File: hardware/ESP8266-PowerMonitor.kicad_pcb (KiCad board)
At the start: 2 copper layers, 31 x 47 mm, 8 parts, among them P1 CONN_01X15, P2 CONN_01X15, P3 CONN_01X02, P4 CONN_01X03, P5 CONN_01X03, P6 CONN_01X03

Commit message: Production prints.
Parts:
- removed the P1 at (143.0, 67.0)
- removed the P2 at (170.0, 67.0)
- removed the P3 at (163.5, 87.5)
- removed the P4 at (150.2, 97.5)
- removed the P5 at (162.5, 97.5)
- removed the P6 at (153.8, 92.8)
- removed the R1 at (153.0, 81.8)
- removed the R2 at (156.2, 81.8)
- added P1: CONN_LEFT, Socket_Strips:Socket_Strip_Straight_1x15, F.Cu at (142.8, 116.8)
- added P1: CONN_LEFT, Socket_Strips:Socket_Strip_Straight_1x15, F.Cu at (177.0, 116.8)
- added P1: CONN_LEFT, Socket_Strips:Socket_Strip_Straight_1x15, F.Cu at (177.2, 68.5)
- added P1: CONN_LEFT, Socket_Strips:Socket_Strip_Straight_1x15, F.Cu at (143.0, 68.5)
- added P2: CONN_RIGHT, Socket_Strips:Socket_Strip_Straight_1x15, F.Cu at (169.5, 116.8)
- added P2: CONN_RIGHT, Socket_Strips:Socket_Strip_Straight_1x15, F.Cu at (203.8, 116.8)
- added P2: CONN_RIGHT, Socket_Strips:Socket_Strip_Straight_1x15, F.Cu at (204.0, 68.5)
- added P2: CONN_RIGHT, Socket_Strips:Socket_Strip_Straight_1x15, F.Cu at (169.8, 68.5)
- added P3: CONN_METER, Pin_Headers:Pin_Header_Straight_1x02, F.Cu at (164.8, 134.8)
- added P3: CONN_METER, Pin_Headers:Pin_Header_Straight_1x02, F.Cu at (199.0, 134.8)
- added P3: CONN_METER, Pin_Headers:Pin_Header_Straight_1x02, F.Cu at (199.2, 86.5)
- added P3: CONN_METER, Pin_Headers:Pin_Header_Straight_1x02, F.Cu at (165.0, 86.5)
- added P4: CONN_PIR, Pin_Headers:Pin_Header_Straight_1x03, F.Cu at (148.5, 121.8)
- added P4: CONN_PIR, Pin_Headers:Pin_Header_Straight_1x03, F.Cu at (182.8, 121.8)
- added P4: CONN_PIR, Pin_Headers:Pin_Header_Straight_1x03, F.Cu at (183.0, 73.5)
- added P4: CONN_PIR, Pin_Headers:Pin_Header_Straight_1x03, F.Cu at (148.8, 73.5)
- added P5: CONN_POWER, Pin_Headers:Pin_Header_Straight_1x03, F.Cu at (148.8, 147.2)
- added P5: CONN_POWER, Pin_Headers:Pin_Header_Straight_1x03, F.Cu at (183.0, 147.2)
- added P5: CONN_POWER, Pin_Headers:Pin_Header_Straight_1x03, F.Cu at (183.2, 99.0)
- added P5: CONN_POWER, Pin_Headers:Pin_Header_Straight_1x03, F.Cu at (149.0, 99.0)
- added P6: CONN_1WIRE, Pin_Headers:Pin_Header_Straight_1x03, F.Cu at (164.8, 143.2)
- added P6: CONN_1WIRE, Pin_Headers:Pin_Header_Straight_1x03, F.Cu at (199.0, 143.2)
- added P6: CONN_1WIRE, Pin_Headers:Pin_Header_Straight_1x03, F.Cu at (199.2, 95.0)
- added P6: CONN_1WIRE, Pin_Headers:Pin_Header_Straight_1x03, F.Cu at (165.0, 95.0)
- added R1: 220, Resistors_ThroughHole:Resistor_Horizontal_RM10mm, F.Cu at (160.5, 143.8)
- added R1: 220, Resistors_ThroughHole:Resistor_Horizontal_RM10mm, F.Cu at (194.8, 143.8)
- added R1: 220, Resistors_ThroughHole:Resistor_Horizontal_RM10mm, F.Cu at (195.0, 95.5)
- added R1: 220, Resistors_ThroughHole:Resistor_Horizontal_RM10mm, F.Cu at (160.8, 95.5)
- added R2: 4.7k, Resistors_ThroughHole:Resistor_Horizontal_RM10mm, F.Cu at (157.2, 143.8)
- added R2: 4.7k, Resistors_ThroughHole:Resistor_Horizontal_RM10mm, F.Cu at (191.5, 143.8)
- added R2: 4.7k, Resistors_ThroughHole:Resistor_Horizontal_RM10mm, F.Cu at (191.8, 95.5)
- added R2: 4.7k, Resistors_ThroughHole:Resistor_Horizontal_RM10mm, F.Cu at (157.5, 95.5)
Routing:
- net GND: track 0.00 -> 209.3 mm
- net 5V: track 0.00 -> 174.1 mm
- net 3.3V: track 0.00 -> 131.7 mm
- net (no net): track 0.00 -> 109.0 mm
- net GPIO5: track 0.00 -> 84.1 mm
- net GPIO0: track 0.00 -> 77.5 mm
- net Net-(P1-Pad14): track 40.5 -> 0.00 mm
- net GPIO15: track 0.00 -> 39.8 mm
- net Net-(P6-Pad2): track 3.52 -> 38.2 mm
- net Net-(P2-Pad15): track 24.9 -> 0.00 mm
- net Net-(P1-Pad15): track 19.5 -> 0.00 mm
- net Net-(P3-Pad2): track 0.00 -> 19.3 mm
- net Net-(P2-Pad11): track 8.48 -> 0.00 mm
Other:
- net class Default: trace_width 0.25 -> 0.5
- net class Outline added: clearance 0.2, trace_width 0.2, via_dia 0.6, via_drill 0.4

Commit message: Updated schematics & PCB.
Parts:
- removed the P1 at (142.8, 116.8)
- removed the P1 at (177.0, 116.8)
- removed the P1 at (177.2, 68.5)
- removed the P2 at (169.5, 116.8)
- removed the P2 at (203.8, 116.8)
- removed the P2 at (204.0, 68.5)
- removed the P3 at (164.8, 134.8)
- removed the P3 at (199.0, 134.8)
- removed the P3 at (199.2, 86.5)
- removed the P4 at (148.5, 121.8)
- removed the P4 at (182.8, 121.8)
- removed the P4 at (183.0, 73.5)
- removed the P5 at (148.8, 147.2)
- removed the P5 at (183.0, 147.2)
- removed the P5 at (183.2, 99.0)
- removed the P6 at (164.8, 143.2)
- removed the P6 at (199.0, 143.2)
- removed the P6 at (199.2, 95.0)
- removed the R1 at (160.5, 143.8)
- removed the R1 at (194.8, 143.8)
- removed the R1 at (195.0, 95.5)
- removed the R2 at (157.2, 143.8)
- removed the R2 at (191.5, 143.8)
- removed the R2 at (191.8, 95.5)
- moved R2 9.10 mm to (166.2, 93.0)
- moved P6 7.63 mm to (161.0, 101.5), turned to 90 degrees
- moved P3 7.59 mm to (162.8, 93.8), turned to 270 degrees
- moved R1 6.01 mm to (155.0, 97.2), turned to 180 degrees
- moved P4 5.46 mm to (147.2, 68.2), turned to 90 degrees
- moved P5 3.05 mm to (147.2, 101.5), turned to 90 degrees
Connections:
- P2 pad 3: Net-(P2-Pad3) -> GPIO4
- P2 pad 4: GPIO0 -> Net-(P2-Pad4)
- P5 pad 2: 3.3V -> 5V
- P5 pad 3: 5V -> 3.3V
- P6 pad 2: Net-(P6-Pad2) -> GPIO4
- R2 pad 1: Net-(P6-Pad2) -> 3.3V
- R2 pad 2: GPIO0 -> GPIO4
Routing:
- net GND: track 209.3 -> 37.5 mm
- net 5V: track 174.1 -> 43.5 mm
- net 3.3V: track 131.7 -> 31.2 mm
- net (no net): track 109.0 -> 26.8 mm
- net GPIO0: track 77.5 -> 0.00 mm
- net GPIO5: track 84.1 -> 23.2 mm
- net GPIO4: track 0.00 -> 41.4 mm
- net Net-(P6-Pad2): track 38.2 -> 0.00 mm
- net GPIO15: track 39.8 -> 7.06 mm
- net Net-(P3-Pad2): track 19.3 -> 3.55 mm

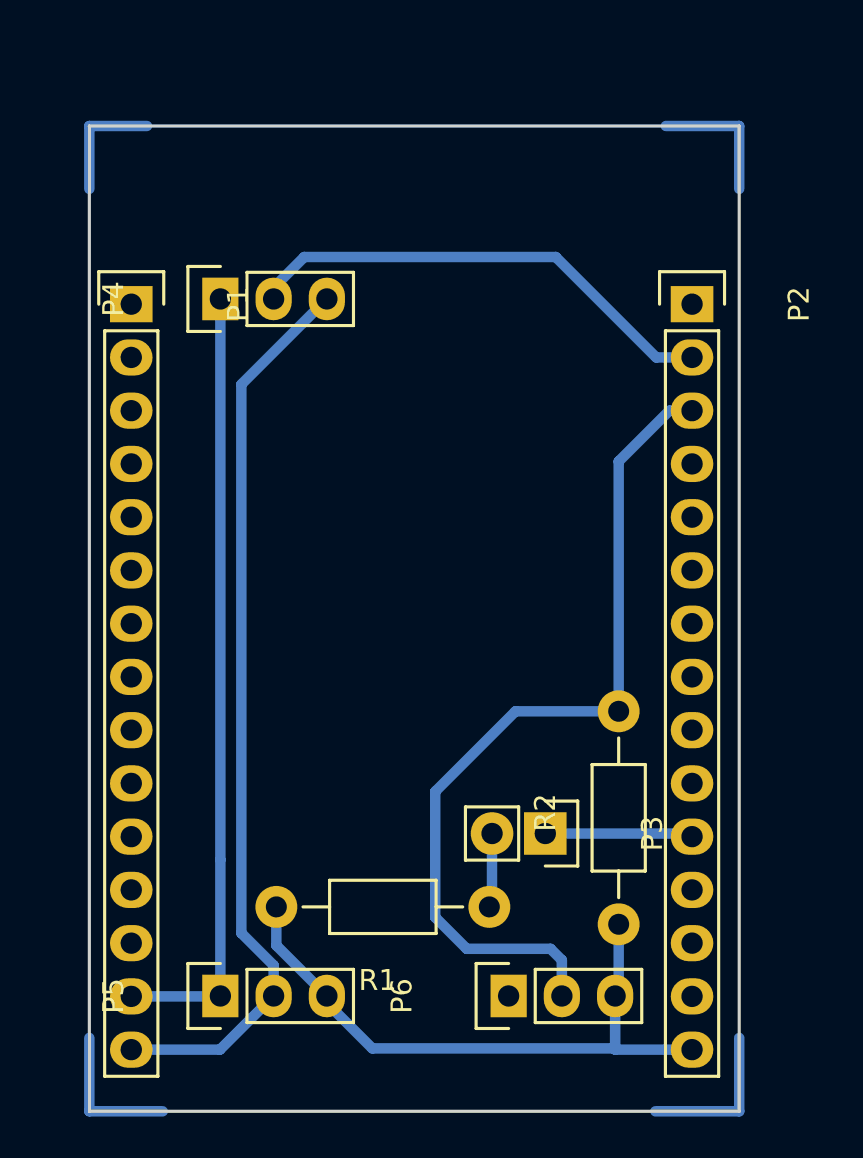
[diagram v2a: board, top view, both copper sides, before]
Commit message: Improved, complete PCB, pre-panelized.
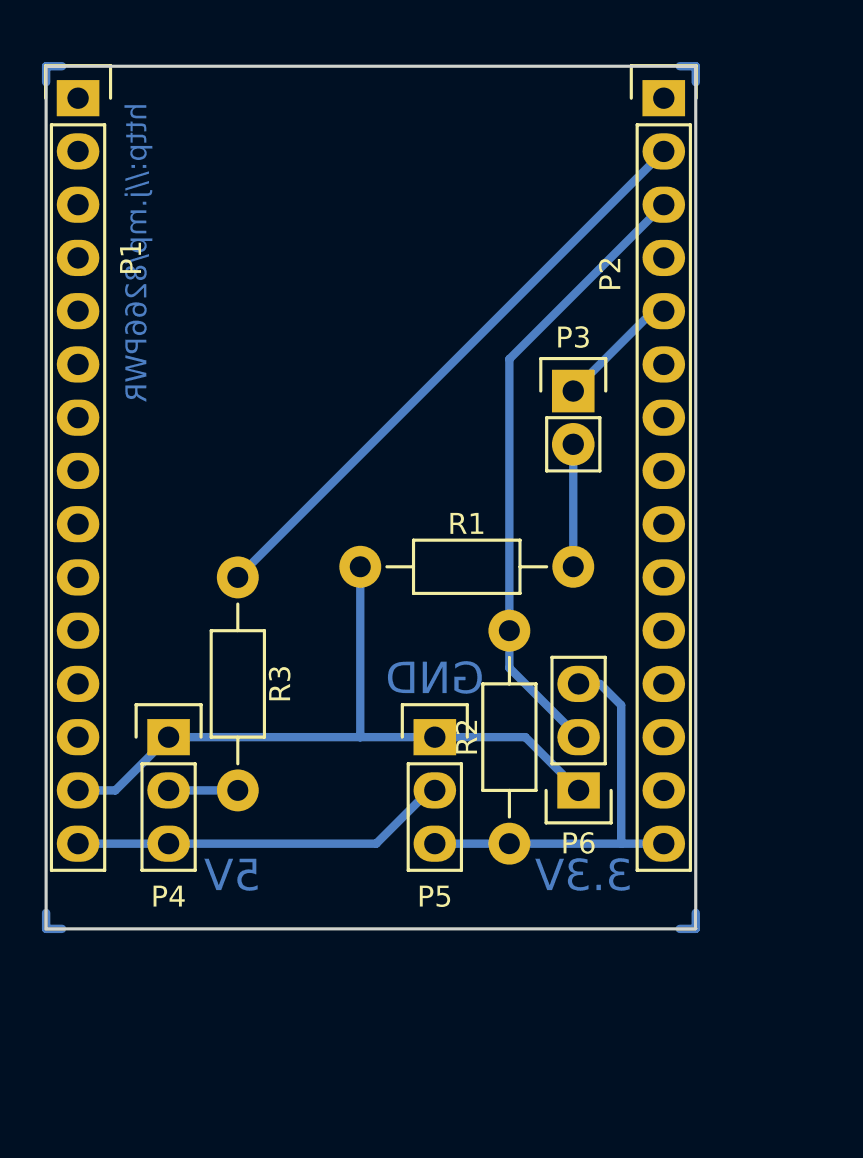
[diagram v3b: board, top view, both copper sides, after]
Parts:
- added R3: 470, Resistors_ThroughHole:Resistor_Horizontal_RM10mm, F.Cu at (148.1, 86.6)
- R1: value 220 -> 470
- R2: value 4.7k -> 2.2k
- moved P3 21.1 mm to (164.1, 72.6), turned to 0 degrees
- moved P4 21.0 mm to (144.8, 89.2), turned to 0 degrees
- moved R1 16.7 mm to (159.0, 81.0)
- moved P5 16.0 mm to (157.5, 89.2), turned to 0 degrees
- moved P6 10.4 mm to (164.3, 91.7), turned to 180 degrees
- moved P1 10.1 mm to (140.5, 58.7)
- moved P2 9.92 mm to (168.4, 58.7)
- moved R2 6.48 mm to (161.0, 89.2)
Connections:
- P2 pad 11: GPIO15 -> Net-(P2-Pad11)
- P2 pad 5: Net-(P2-Pad5) -> GPIO2
- P3 pad 1: GPIO15 -> GPIO2
- P4 pad 2: GPIO5 -> Net-(P4-Pad2)
- R1 pad 2: 3.3V -> GND
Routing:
- net 5V: track 43.5 -> 18.4 mm
- net (no net): track 26.8 -> 6.10 mm
- net 3.3V: track 31.2 -> 20.0 mm
- net GPIO4: track 41.4 -> 30.3 mm
- net GPIO15: track 7.06 -> 0.00 mm
- net GPIO2: track 0.00 -> 5.90 mm
- net GPIO5: track 23.2 -> 28.7 mm
- net GND: track 37.5 -> 34.1 mm
- net Net-(P4-Pad2): track 0.00 -> 3.30 mm
- net Net-(P3-Pad2): track 3.55 -> 5.84 mm
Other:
- board size 31 x 47 mm -> 31 x 41.1 mm
- net class Copper Outline added: clearance 0.2, trace_width 0.2, via_dia 0.6, via_drill 0.4
- net class Default: trace_width 0.5 -> 0.4
- board text added: "3.3V"
- board text added: "5V"
- board text added: "GND"
- board text added: "http://j.mp/8266PWR"

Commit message: Redesigned the board.
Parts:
- removed P1: CONN_LEFT, Socket_Strips:Socket_Strip_Straight_1x15
- removed P2: CONN_RIGHT, Socket_Strips:Socket_Strip_Straight_1x15
- removed P3: CONN_METER, Pin_Headers:Pin_Header_Straight_1x02
- removed P4: CONN_PIR, Pin_Headers:Pin_Header_Straight_1x03
- removed P5: CONN_POWER, Pin_Headers:Pin_Header_Straight_1x03
- removed P6: CONN_1WIRE, Pin_Headers:Pin_Header_Straight_1x03
- added C1: 0.1uF, Capacitor_SMD:C_1206_3216Metric_Pad1.42x1.75mm_HandSolder, B.Cu at (139.4, 100.9)
- added C2: 10uF, Capacitor_SMD:CP_Elec_4x5.3, F.Cu at (151.5, 108.0)
- added C3: 100nF, Capacitor_SMD:C_1206_3216Metric_Pad1.42x1.75mm_HandSolder, F.Cu at (149.7, 100.8)
- added F1: 100mA, Fuse:Fuse_1206_3216Metric_Pad1.42x1.75mm_HandSolder, F.Cu at (118.0, 99.9)
- added J1: CONN_PULSE, Connector_PinHeader_2.54mm:PinHeader_1x02_P2.54mm_Vertical, F.Cu at (152.9, 115.9)
- added J2: CONN_PROG, Connector_PinHeader_2.54mm:PinHeader_1x05_P2.54mm_Vertical, F.Cu at (165.7, 116.1)
- added J3: CONN_AC, TerminalBlock:TerminalBlock_bornier-2_P5.08mm, F.Cu at (123.5, 113.8)
- added J4: CONN_TEMP, Connector_PinHeader_2.54mm:PinHeader_1x03_P2.54mm_Vertical, F.Cu at (149.1, 115.9)
- added JP1: 3.3V BYPASS, Jumper:SolderJumper-2_P1.3mm_Open_TrianglePad1.0x1.5mm, F.Cu at (144.5, 104.3)
- added PS1: HLK-PM03, Converter_ACDC:Converter_ACDC_HiLink_HLK-PMxx, F.Cu at (110.1, 98.5)
- added R4: 10k, Resistor_SMD:R_1206_3216Metric_Pad1.42x1.75mm_HandSolder, B.Cu at (168.5, 104.5)
- added R5: 10k, Resistor_SMD:R_1206_3216Metric_Pad1.42x1.75mm_HandSolder, B.Cu at (165.7, 104.5)
- added R6: 10k, Resistor_SMD:R_1206_3216Metric_Pad1.42x1.75mm_HandSolder, F.Cu at (160.7, 115.8)
- added REF**: , MountingHole:MountingHole_2.2mm_M2, F.Cu at (117.6, 113.7)
- added SW1: SW_RESET, Button_Switch_SMD:SW_Push_1P1T_NO_6x6mm_H9.5mm, F.Cu at (155.6, 96.8)
- added U1: AMS1117-3.3, Package_TO_SOT_SMD:SOT-223-3_TabPin2, F.Cu at (147.3, 95.5)
- added U2: ESP-12F, RF_Module:ESP-12E, F.Cu at (172.2, 103.4)
- R1: value 470 -> 10k; footprint Resistors_ThroughHole:Resistor_Horizontal_RM10mm -> Resistor_SMD:R_1206_3216Metric_Pad1.42x1.75mm_HandSolder
- R2: value 2.2k -> 10k; footprint Resistors_ThroughHole:Resistor_Horizontal_RM10mm -> Resistor_SMD:R_1206_3216Metric_Pad1.42x1.75mm_HandSolder
- R3: footprint Resistors_ThroughHole:Resistor_Horizontal_RM10mm -> Resistor_SMD:R_1206_3216Metric_Pad1.42x1.75mm_HandSolder; moved to B.Cu
- moved R3 29.4 mm to (171.4, 104.5)
- moved R1 12.0 mm to (161.3, 92.8), turned to 0 degrees
- moved R2 6.56 mm to (166.5, 92.8), turned to 0 degrees
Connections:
- R1 pad 2: GND -> +3.3V
- R2 pad 1: 3.3V -> +3.3V
- R2 pad 2: GPIO4 -> Net-(R2-Pad2)
- R3 pad 2: GPIO5 -> PULSE
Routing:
- net +3.3V: track 0.00 -> 78.6 mm, vias 0 -> 1
- net GND: track 34.1 -> 68.7 mm
- net GPIO4: track 30.3 -> 0.00 mm
- net GPIO5: track 28.7 -> 0.00 mm
- net DS18B20_DQ: track 0.00 -> 27.9 mm, vias 0 -> 1
- net PULSE: track 0.00 -> 24.6 mm
- net 3.3V: track 20.0 -> 0.00 mm
- net Net-(C1-Pad1): track 0.00 -> 19.2 mm
- net AC-N: track 0.00 -> 18.8 mm
- net 5V: track 18.4 -> 0.00 mm
- net AC-L: track 0.00 -> 16.8 mm
- net Net-(R1-Pad1): track 5.84 -> 21.7 mm
- net _PROG: track 0.00 -> 15.6 mm
- net Net-(R5-Pad2): track 0.00 -> 8.62 mm, vias 0 -> 1
- net Net-(F1-Pad1): track 0.00 -> 7.92 mm
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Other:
- board size 31 x 41.1 mm -> 69.5 x 27.2 mm
- board text added: "0,8"
- board text added: "0,9"
- board text added: "10"
- board text added: "12,6"
- board text added: "17,9"
- board text added: "26,65"
- board text added: "27,1"
- board text added: "27,15"
- board text added: "28,85"
- board text added: "3,45"
- board text added: "30,95"
- board text added: "35,2"
- board text added: "5,35"
- board text added: "63,05"
- board text added: "7,05"
- board text added: "7,35"
- board text added: "72,1"
- board text added: "8,4"
- board text added: "90"
- board text added: "A"
- board text added: "gitlab.com/ jasiek/ ESP8266-PowerMonitor"
- board text removed: "3.3V"
- board text removed: "5V"
- board text removed: "GND"
- board text removed: "http://j.mp/8266PWR"

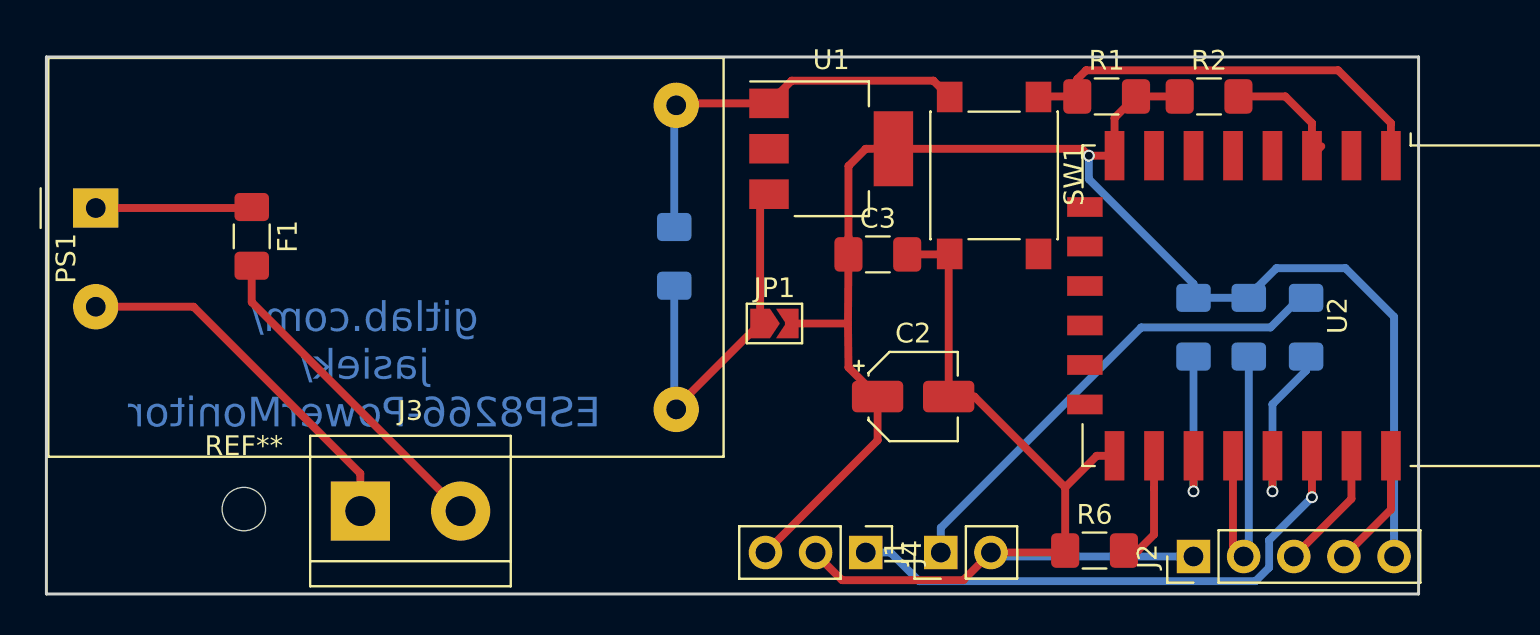
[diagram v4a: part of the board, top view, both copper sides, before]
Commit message: * Reworked the board to use 0.5/1.3mm vias. * Added I2C to GPIO4/5 in case we want to use an OLED display. * Moved the pulse pin to GPIO2 (pulled up). * Re-orged the board to use fewer vias.
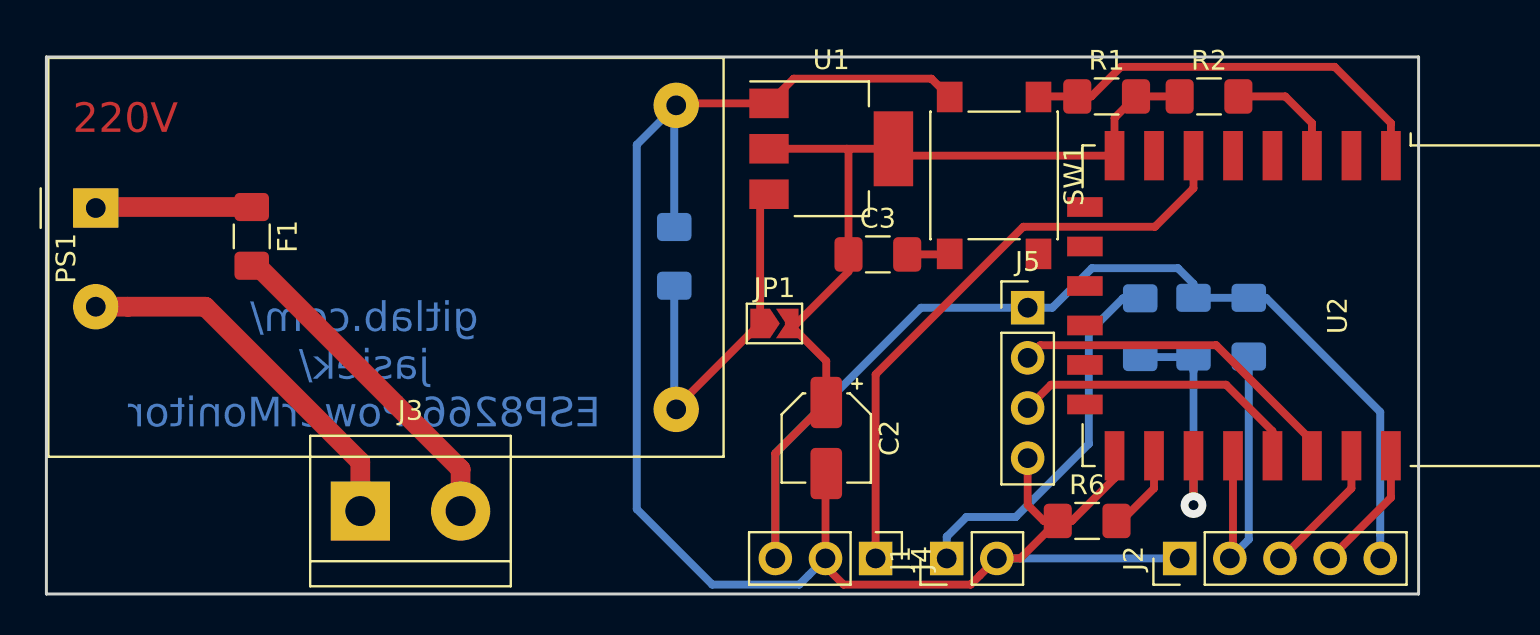
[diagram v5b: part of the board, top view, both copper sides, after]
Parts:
- removed REF**: , MountingHole:MountingHole_2.2mm_M2
- added J5: CONN_I2C, Connector_PinHeader_2.54mm:PinHeader_1x04_P2.54mm_Vertical, F.Cu at (157.3, 103.5)
- moved R3 8.40 mm to (163.0, 104.5)
- moved C2 4.88 mm to (147.1, 110.1), turned to 270 degrees
- moved R6 1.55 mm to (160.3, 114.3)
- moved J2 0.71 mm to (165.0, 116.2)
- moved J4 0.58 mm to (149.6, 116.2)
- moved J1 0.42 mm to (153.2, 116.2)
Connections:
- R5 pad 2: Net-(R5-Pad2) -> Net-(R3-Pad1)
- U2 pad 17: Net-(R5-Pad2) -> Net-(R3-Pad1)
- U2 pad 19: Net-(R3-Pad1) -> SDA
- U2 pad 20: DS18B20_DQ -> SCL
- U2 pad 6: (no net) -> DS18B20_DQ
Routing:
- net GND: track 68.7 -> 92.7 mm
- net +3.3V: track 78.6 -> 98.1 mm, vias 1 -> 0
- net SCL: track 0.00 -> 17.4 mm
- net SDA: track 0.00 -> 15.9 mm
- net Net-(R5-Pad2): track 8.62 -> 0.00 mm, vias 1 -> 0
- net PULSE: track 24.6 -> 19.2 mm
- net Net-(R3-Pad1): track 9.33 -> 12.7 mm
- net DS18B20_DQ: track 27.9 -> 31.0 mm, vias 1 -> 0
- net Net-(R6-Pad2): track 5.85 -> 4.23 mm
- net _PROG: track 15.6 -> 16.2 mm
- net Net-(R2-Pad2): track 6.61 -> 5.93 mm
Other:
- net class AC added: clearance 1, trace_width 1, via_dia 1.3, via_drill 0.5
- net class Default: via_dia 0.6 -> 1.3; via_drill 0.4 -> 0.5
- board text added: "220V~"
